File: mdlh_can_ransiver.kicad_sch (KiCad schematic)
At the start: 28 parts, among them U1 MCP2515-xSO, U2 MCP2551-I-SN, Y1 16MHz

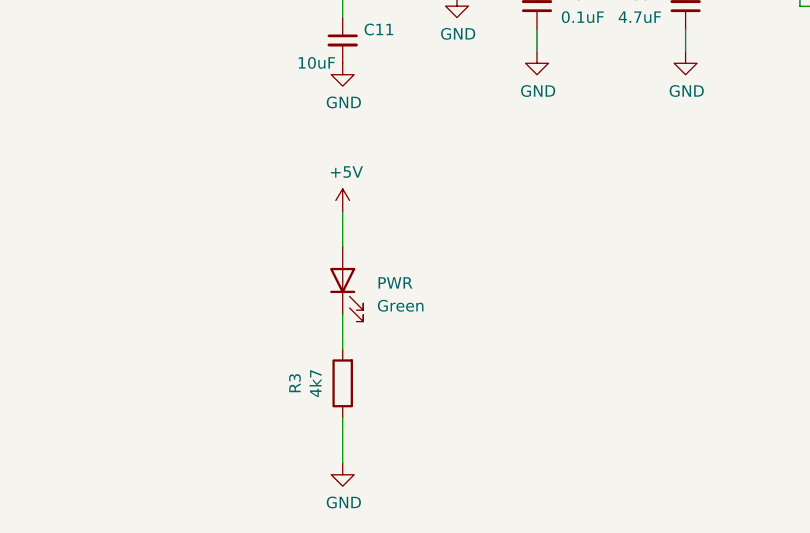
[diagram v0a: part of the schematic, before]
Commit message: Add PCA9306 i2c transciever
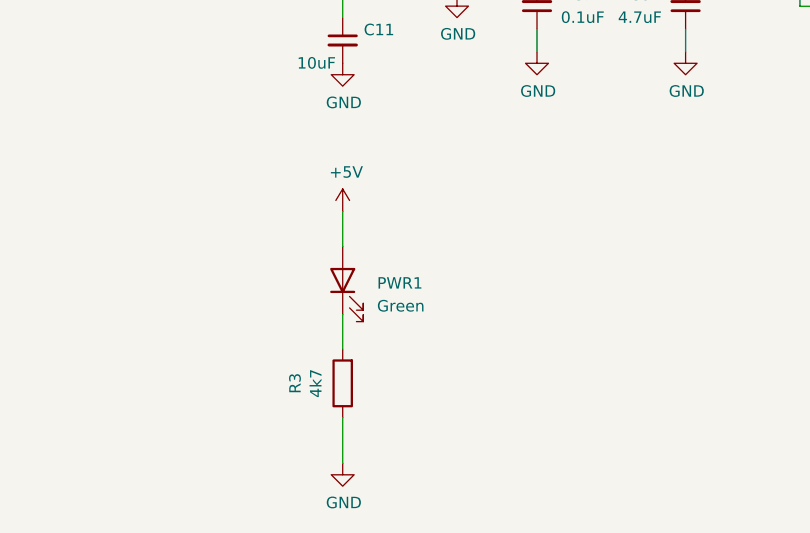
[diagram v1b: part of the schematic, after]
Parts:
- R3: footprint Resistor_SMD:R_0603_1608Metric -> Resistor_SMD:R_0805_2012Metric_Pad1.20x1.40mm_HandSolder
- renumbered PWR to PWR1
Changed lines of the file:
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@@
       (effects (font (size 1.27 1.27)))
     )
-    (property "Footprint" "Resistor_SMD:R_0603_1608Metric" (at 246.888 85.09 90)
+    (property "Footprint" "Resistor_SMD:R_0805_2012Metric_Pad1.20x1.40mm_HandSolder" (at 246.888 85.09 90)
       (effects (font (size 1.27 1.27)) hide)
     )
@@
   (symbol (lib_id "Device:LED") (at 176.53 129.54 90) (unit 1)
     (in_bom yes) (on_board yes) (dnp no) (fields_autoplaced)
-    (property "Reference" "PWR" (at 180.34 129.8575 90)
+    (property "Reference" "PWR1" (at 180.34 129.8575 90)
       (effects (font (size 1.27 1.27)) (justify right))
     )
@@
       (project "ltp_kikad"
         (path "/eed35b77-cbf9-4596-9b17-2558f81058ba/d18f2354-5f56-48bf-919b-3fdf8c87b820"
-          (reference "PWR") (unit 1)
-        )
-      )
+          (reference "PWR1") (unit 1)
+        )
+      )

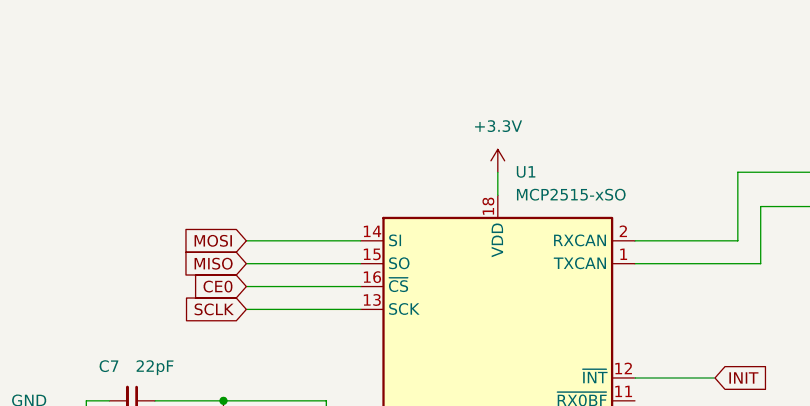
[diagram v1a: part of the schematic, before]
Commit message: Add testpoints
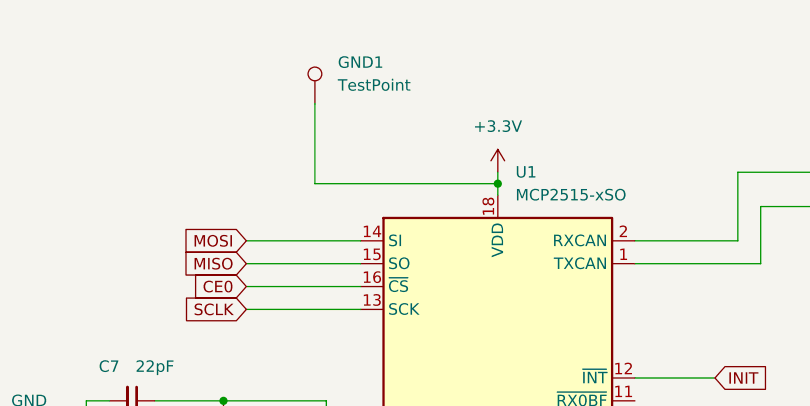
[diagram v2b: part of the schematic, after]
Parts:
- added GND1: TestPoint, TestPoint:TestPoint_Pad_D1.0mm, symbol Connector:TestPoint
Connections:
- net +3.3V: now also GND1.1
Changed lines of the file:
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@@
   (junction (at 62.23 102.87) (diameter 0) (color 0 0 0 0)
   )
+  (junction (at 92.71 71.12) (diameter 0) (color 0 0 0 0)
+  )
   (junction (at 62.23 95.25) (diameter 0) (color 0 0 0 0)
   )
@@
     (stroke (width 0) (type default))
   )
-  (wire (pts (xy 92.71 69.85) (xy 92.71 72.39))
+  (wire (pts (xy 92.71 69.85) (xy 92.71 71.12))
     (stroke (width 0) (type default))
   )
@@
     (stroke (width 0) (type default))
   )
+  (wire (pts (xy 72.39 71.12) (xy 92.71 71.12))
+    (stroke (width 0) (type default))
+  )
   (wire (pts (xy 207.01 85.09) (xy 207.01 87.63))
     (stroke (width 0) (type default))
@@
     (stroke (width 0) (type default))
   )
+  (wire (pts (xy 72.39 62.23) (xy 72.39 71.12))
+    (stroke (width 0) (type default))
+  )
   (wire (pts (xy 46.99 99.06) (xy 46.99 102.87))
     (stroke (width 0) (type default))
@@
   )
   (wire (pts (xy 157.48 73.66) (xy 161.29 73.66))
+    (stroke (width 0) (type default))
+  )
+  (wire (pts (xy 92.71 71.12) (xy 92.71 72.39))
     (stroke (width 0) (type default))
   )
@@
         )
       )
+    )
+  )
+  (symbol (lib_id "Connector:TestPoint") (at 72.39 62.23 0) (unit 1)
+    (in_bom yes) (on_board yes) (dnp no) (fields_autoplaced)
+    (property "Reference" "GND1" (at 74.93 57.658 0)
+      (effects (font (size 1.27 1.27)) (justify left))
+    )
+    (property "Value" "TestPoint" (at 74.93 60.198 0)
+      (effects (font (size 1.27 1.27)) (justify left))
+    )
+    (property "Footprint" "TestPoint:TestPoint_Pad_D1.0mm" (at 77.47 62.23 0)
+      (effects (font (size 1.27 1.27)) hide)
+    )
+    (property "Datasheet" "~" (at 77.47 62.23 0)
+      (effects (font (size 1.27 1.27)) hide)
+    )
+    (pin "1")
+    (instances
+      (project "ltp_kikad"
+        (path "/eed35b77-cbf9-4596-9b17-2558f81058ba/2fb8f433-d537-4253-8cc8-f6d42368ed9e"
+          (reference "GND1") (unit 1)
+        )
+        (path "/eed35b77-cbf9-4596-9b17-2558f81058ba/7d22e16e-a0ba-4766-b1de-c8cbb28f14f7"
+          (reference "+5v1") (unit 1)
+        )
+        (path "/eed35b77-cbf9-4596-9b17-2558f81058ba/d18f2354-5f56-48bf-919b-3fdf8c87b820"
+          (reference "+3.3v1") (unit 1)
+        )
+      )
